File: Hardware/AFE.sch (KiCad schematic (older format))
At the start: 46 parts, among them U801 4069.HEF4069UBTT,118, U802 MCP47CXBX2

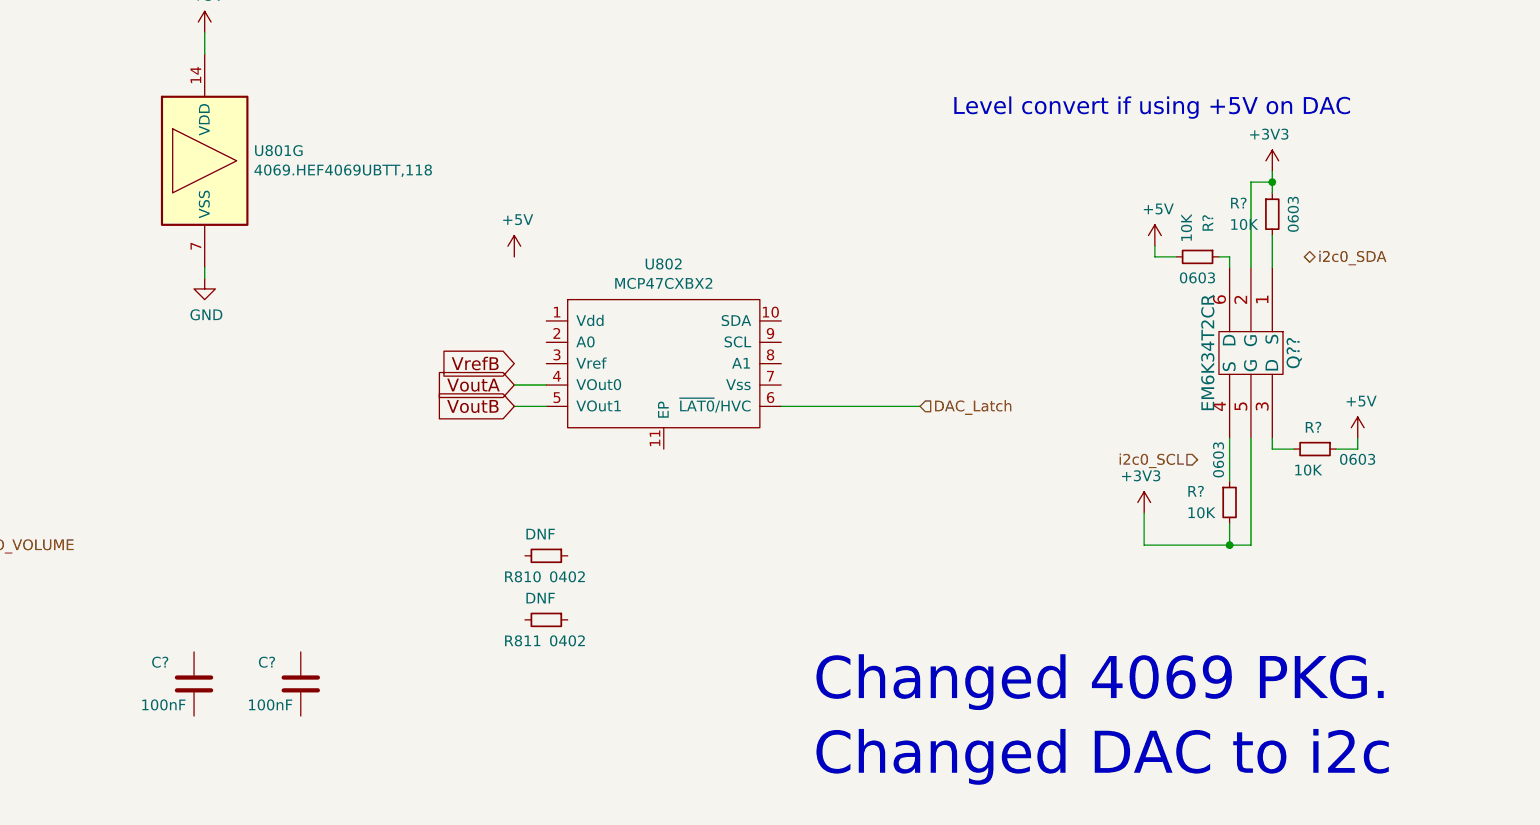
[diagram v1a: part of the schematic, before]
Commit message: Hooking up switches, some more connectivity.
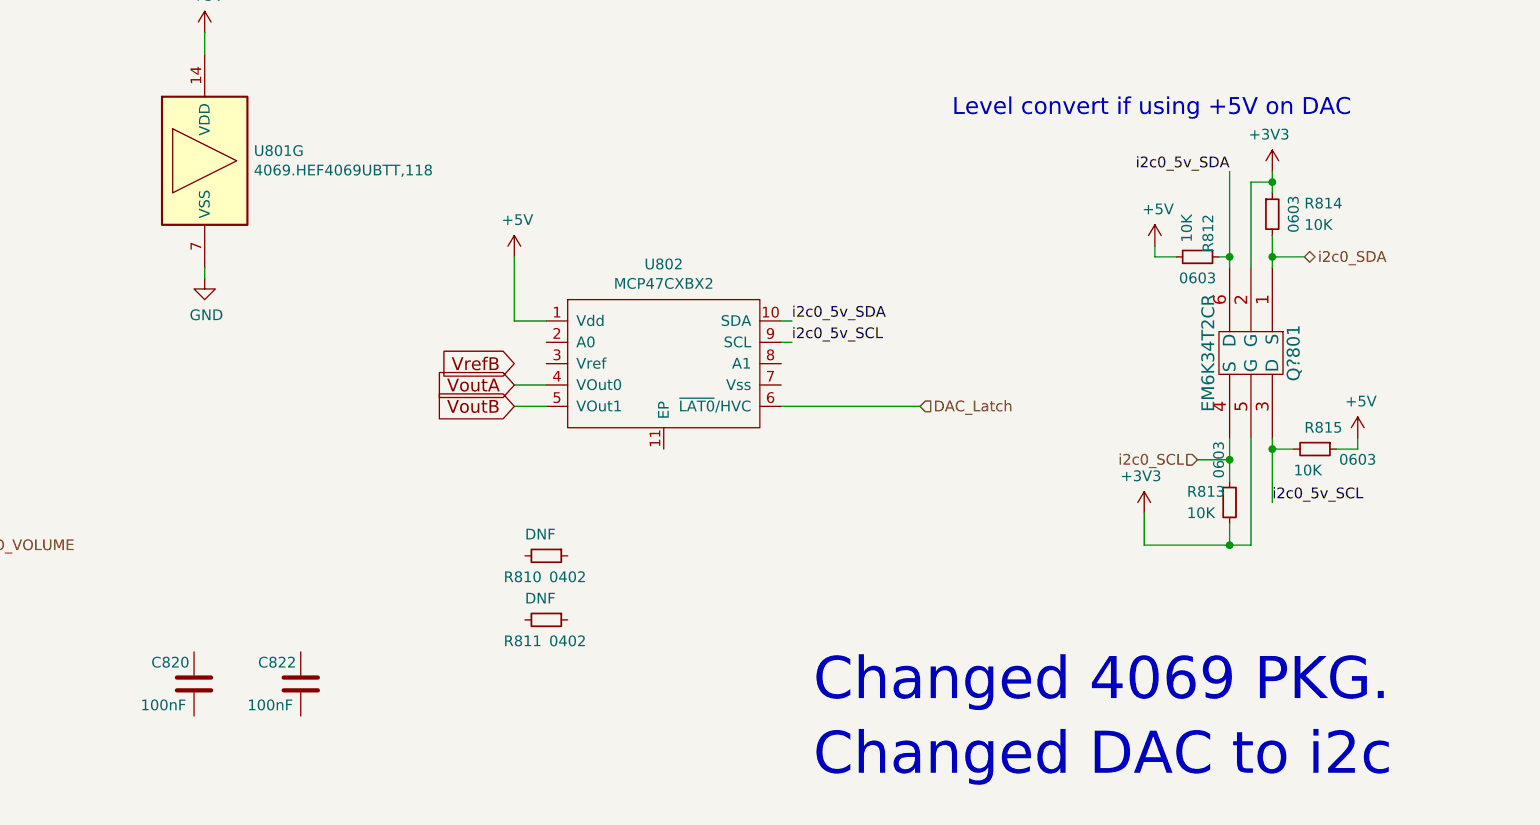
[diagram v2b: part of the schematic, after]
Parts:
- gave numbers to parts that had none: 7
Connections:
- net +5V: now also U802.1 (Vdd)
- net i2c0_SCL: now also Q?801.4 (S), R813.1
- net i2c0_SDA: now also Q?801.1 (S), R814.2
- net i2c0_5v_SDA: now reaches U802.10 (SDA)
- net i2c0_5v_SDA: now also Q?801.6 (D), R812.1
- net i2c0_5v_SCL: now reaches U802.9 (SCL)
- net i2c0_5v_SCL: now also Q?801.3 (D), R815.2
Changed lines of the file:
@@
 	1050 6900 1050 7000
 $Comp
-L OHMC2022:EM6K34T2CR Q??
+L OHMC2022:EM6K34T2CR Q?801
 U 1 1 613FBC97
 P 10200 4350
-F 0 "Q??" H 10200 4550 60  0000 C CNN
+F 0 "Q?801" H 10200 4550 60  0000 C CNN
 F 1 "EM6K34T2CR" H 10200 4150 60  0000 C CNN
 F 2 "OHMC2022:DualNFet.SOT563.EM6K34T2CR" H 11200 4590 60  0001 C CNN
@@
 $EndComp
 $Comp
-L Device:C C?
+L Device:C C822
 U 1 1 6140B8D2
 P 5750 5900
-F 0 "C?" H 5550 6000 50  0000 L CNN
+F 0 "C822" H 5550 6000 50  0000 L CNN
 F 1 "100nF" H 5500 5800 50  0000 L CNN
 F 2 "Capacitor_SMD:C_0603_1608Metric_Pad1.08x0.95mm_HandSolder" H 5788 5750 50  0001 C CNN
@@
 $EndComp
 $Comp
-L Device:C C?
+L Device:C C820
 U 1 1 6140CB4F
 P 5250 5900
-F 0 "C?" H 5050 6000 50  0000 L CNN
+F 0 "C820" H 5050 6000 50  0000 L CNN
 F 1 "100nF" H 5000 5800 50  0000 L CNN
 F 2 "Capacitor_SMD:C_0603_1608Metric_Pad1.08x0.95mm_HandSolder" H 5288 5750 50  0001 C CNN
@@
 AR Path="/611E335F/614210B0" Ref="R?"  Part="1"
 AR Path="/614210B0" Ref="R?"  Part="1"
-AR Path="/612429E8/614210B0" Ref="R?"  Part="1"
-F 0 "R?" H 10100 3750 50  0000 L CNN
-F 1 "10K" H 10100 3650 50  0000 L CNN
+AR Path="/612429E8/614210B0" Ref="R814"  Part="1"
+F 0 "R814" H 10450 3750 50  0000 L CNN
+F 1 "10K" H 10450 3650 50  0000 L CNN
 F 2 "Resistor_SMD:R_0603_1608Metric" V 10230 3700 50  0001 C CNN
 F 3 "~" H 10300 3700 50  0001 C CNN
@@
 AR Path="/611E335F/614261D7" Ref="R?"  Part="1"
 AR Path="/614261D7" Ref="R?"  Part="1"
-AR Path="/612429E8/614261D7" Ref="R?"  Part="1"
-F 0 "R?" H 9750 3950 50  0000 L CNN
+AR Path="/612429E8/614261D7" Ref="R812"  Part="1"
+F 0 "R812" H 9750 3950 50  0000 L CNN
 F 1 "10K" H 9750 3850 50  0000 L CNN
 F 2 "Resistor_SMD:R_0603_1608Metric" V 9880 3900 50  0001 C CNN
@@
 AR Path="/611E335F/61426AF8" Ref="R?"  Part="1"
 AR Path="/61426AF8" Ref="R?"  Part="1"
-AR Path="/612429E8/61426AF8" Ref="R?"  Part="1"
-F 0 "R?" V 10400 4750 50  0000 L CNN
+AR Path="/612429E8/61426AF8" Ref="R815"  Part="1"
+F 0 "R815" V 10400 4750 50  0000 L CNN
 F 1 "10K" V 10600 4700 50  0000 L CNN
 F 2 "Resistor_SMD:R_0603_1608Metric" V 10430 4800 50  0001 C CNN
@@
 AR Path="/611E335F/61427521" Ref="R?"  Part="1"
 AR Path="/61427521" Ref="R?"  Part="1"
-AR Path="/612429E8/61427521" Ref="R?"  Part="1"
-F 0 "R?" H 9900 5100 50  0000 L CNN
+AR Path="/612429E8/61427521" Ref="R813"  Part="1"
+F 0 "R813" H 9900 5100 50  0000 L CNN
 F 1 "10K" H 9900 5000 50  0000 L CNN
 F 2 "Resistor_SMD:R_0603_1608Metric" V 10030 5050 50  0001 C CNN
@@
 AR Path="/6123BB15/6142CCFA" Ref="#PWR?"  Part="1"
 AR Path="/611E335F/6142CCFA" Ref="#PWR?"  Part="1"
-AR Path="/612429E8/6142CCFA" Ref="#PWR?"  Part="1"
-F 0 "#PWR?" H 6750 3750 50  0001 C CNN
+AR Path="/612429E8/6142CCFA" Ref="#PWR0145"  Part="1"
+F 0 "#PWR0145" H 6750 3750 50  0001 C CNN
 F 1 "+5V" H 6765 4073 50  0000 C CNN
 F 2 "" H 6750 3900 50  0001 C CNN
@@
 AR Path="/6123BB15/6143609C" Ref="#PWR?"  Part="1"
 AR Path="/611E335F/6143609C" Ref="#PWR?"  Part="1"
-AR Path="/612429E8/6143609C" Ref="#PWR?"  Part="1"
-F 0 "#PWR?" H 10700 4600 50  0001 C CNN
+AR Path="/612429E8/6143609C" Ref="#PWR0146"  Part="1"
+F 0 "#PWR0146" H 10700 4600 50  0001 C CNN
 F 1 "+5V" H 10715 4923 50  0000 C CNN
 F 2 "" H 10700 4750 50  0001 C CNN
@@
 AR Path="/6123BB15/61436B56" Ref="#PWR?"  Part="1"
 AR Path="/611E335F/61436B56" Ref="#PWR?"  Part="1"
-AR Path="/612429E8/61436B56" Ref="#PWR?"  Part="1"
-F 0 "#PWR?" H 9750 3700 50  0001 C CNN
+AR Path="/612429E8/61436B56" Ref="#PWR0147"  Part="1"
+F 0 "#PWR0147" H 9750 3700 50  0001 C CNN
 F 1 "+5V" H 9765 4023 50  0000 C CNN
 F 2 "" H 9750 3850 50  0001 C CNN
@@
 AR Path="/611E3335/614785EE" Ref="#PWR?"  Part="1"
 AR Path="/614785EE" Ref="#PWR?"  Part="1"
-F 0 "#PWR?" H 9700 4950 50  0001 C CNN
+AR Path="/612429E8/614785EE" Ref="#PWR0148"  Part="1"
+F 0 "#PWR0148" H 9700 4950 50  0001 C CNN
 F 1 "+3V3" H 9715 5273 50  0000 C CNN
 F 2 "" H 9700 5100 50  0001 C CNN
@@
 AR Path="/611E3335/6147DD9F" Ref="#PWR?"  Part="1"
 AR Path="/6147DD9F" Ref="#PWR?"  Part="1"
-F 0 "#PWR?" H 10300 3350 50  0001 C CNN
+AR Path="/612429E8/6147DD9F" Ref="#PWR0149"  Part="1"
+F 0 "#PWR0149" H 10300 3350 50  0001 C CNN
 F 1 "+3V3" H 10315 3673 50  0000 C CNN
 F 2 "" H 10300 3500 50  0001 C CNN
@@
 	10100 5250 10100 5150
 Wire Wire Line
-	10100 4950 10100 4750
+	10100 4950 10100 4850
 Wire Wire Line
 	10200 4750 10200 5250
@@
 	10300 3550 10300 3600
 Wire Wire Line
-	10300 3800 10300 3950
+	10300 3800 10300 3900
+Wire Wire Line
+	6900 4200 6750 4200
+Wire Wire Line
+	6750 3900 6750 4200
+Wire Wire Line
+	9950 4850 10100 4850
+Connection ~ 10100 4850
+Wire Wire Line
+	10100 4850 10100 4750
+Wire Wire Line
+	10450 3900 10300 3900
+Connection ~ 10300 3900
+Wire Wire Line
+	10300 3900 10300 3950
+Text Label 8050 4300 0    50   ~ 0
+i2c0_5v_SCL
+Text Label 8050 4200 0    50   ~ 0
+i2c0_5v_SDA
+Wire Wire Line
+	8000 4300 8050 4300
+Wire Wire Line
+	8000 4200 8050 4200
+Text Label 10100 3500 2    50   ~ 0
+i2c0_5v_SDA
+Wire Wire Line
+	10100 3500 10100 3900
+Connection ~ 10100 3900
+Text Label 10300 5050 0    50   ~ 0
+i2c0_5v_SCL
+Wire Wire Line
+	10300 5050 10300 4800
+Connection ~ 10300 4800
 $EndSCHEMATC

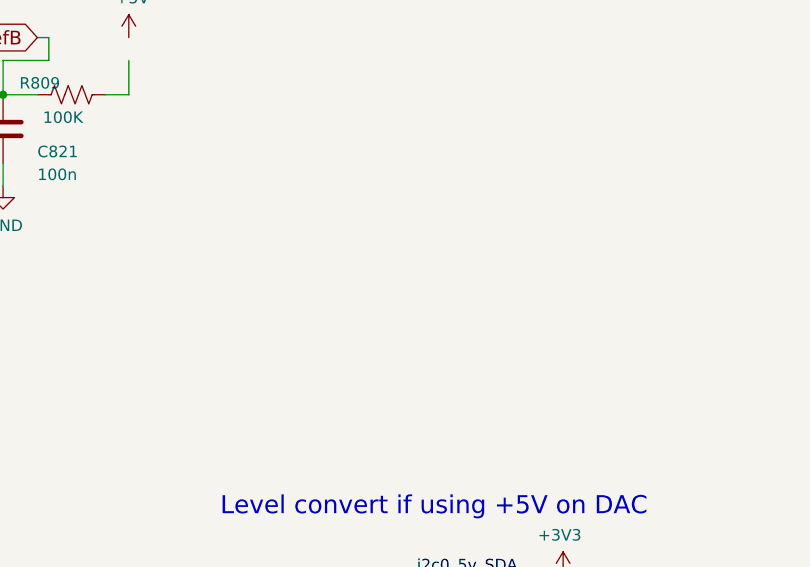
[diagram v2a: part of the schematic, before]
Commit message: Wiring up FPGA, picking pins.
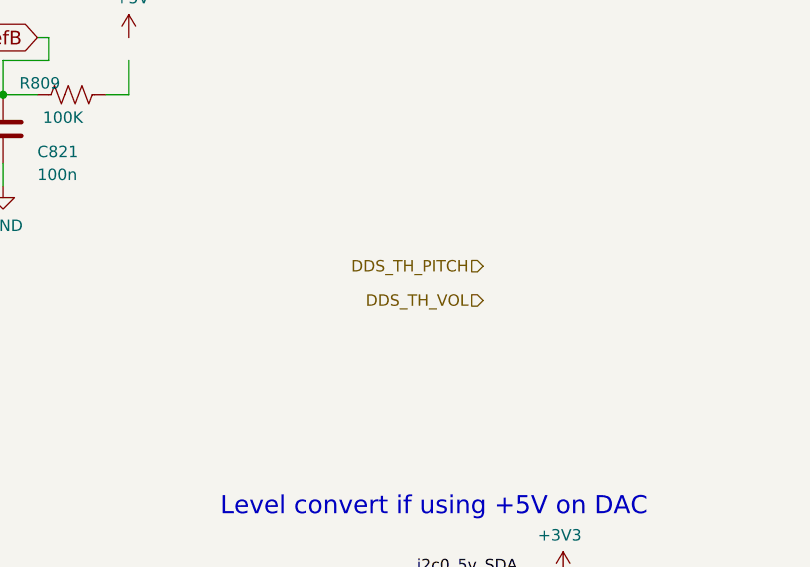
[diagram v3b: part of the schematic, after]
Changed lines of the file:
@@
 	10300 5050 10300 4800
 Connection ~ 10300 4800
+Text HLabel 9950 2150 0    50   Input ~ 0
+DDS_TH_PITCH
+Text HLabel 9950 2300 0    50   Input ~ 0
+DDS_TH_VOL
 $EndSCHEMATC

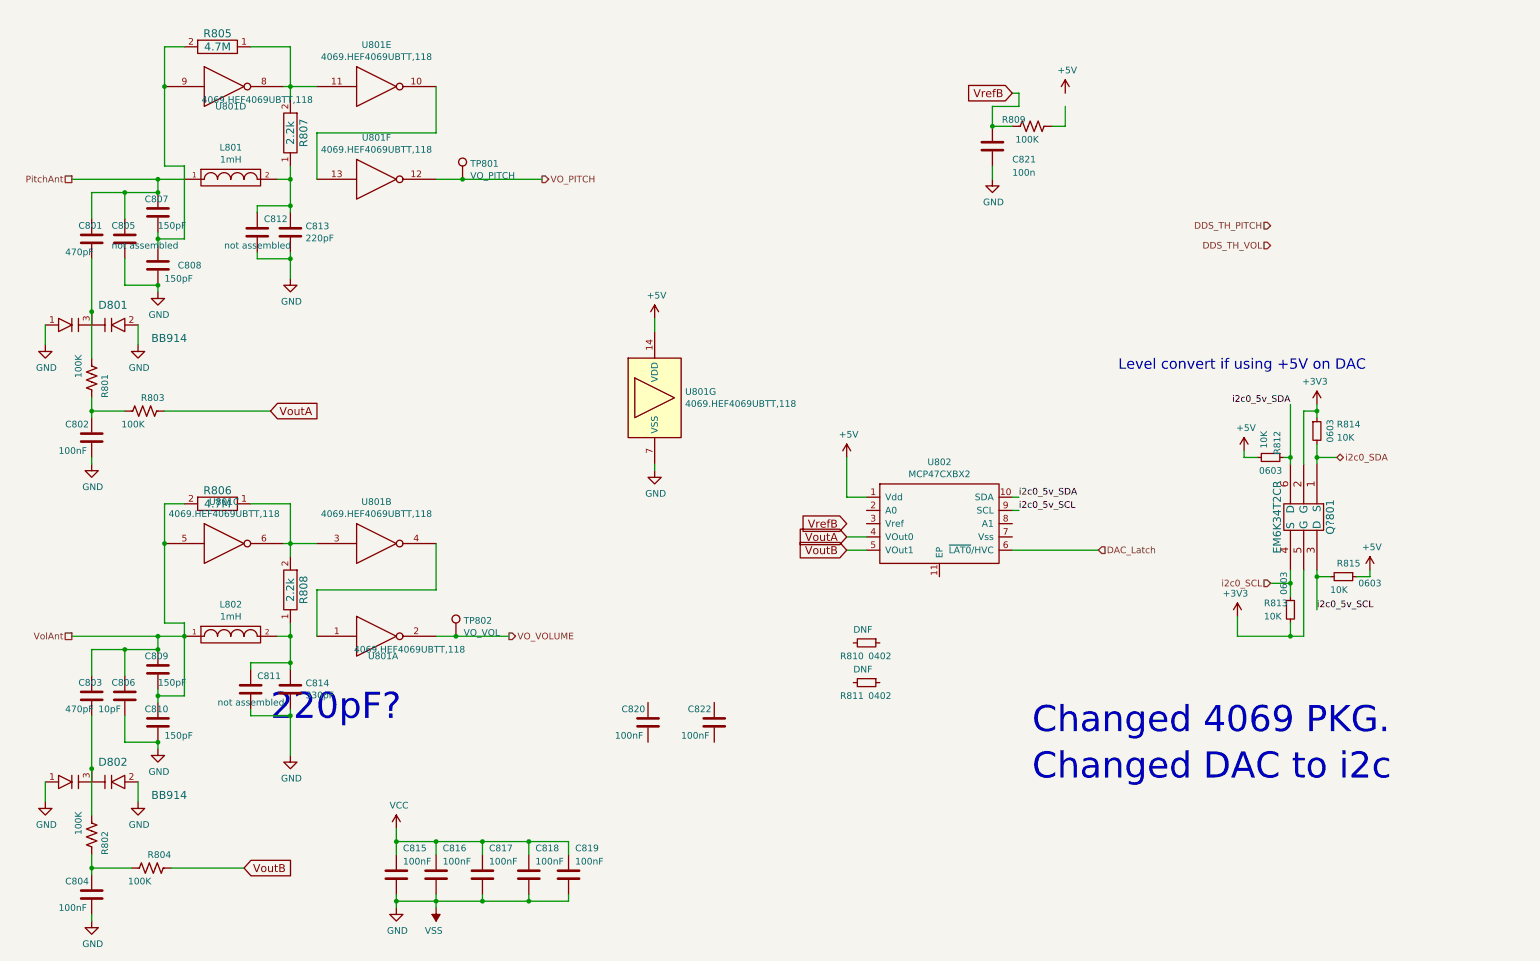
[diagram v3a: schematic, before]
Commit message: Schematic has proposed pin mapping on FPGA.
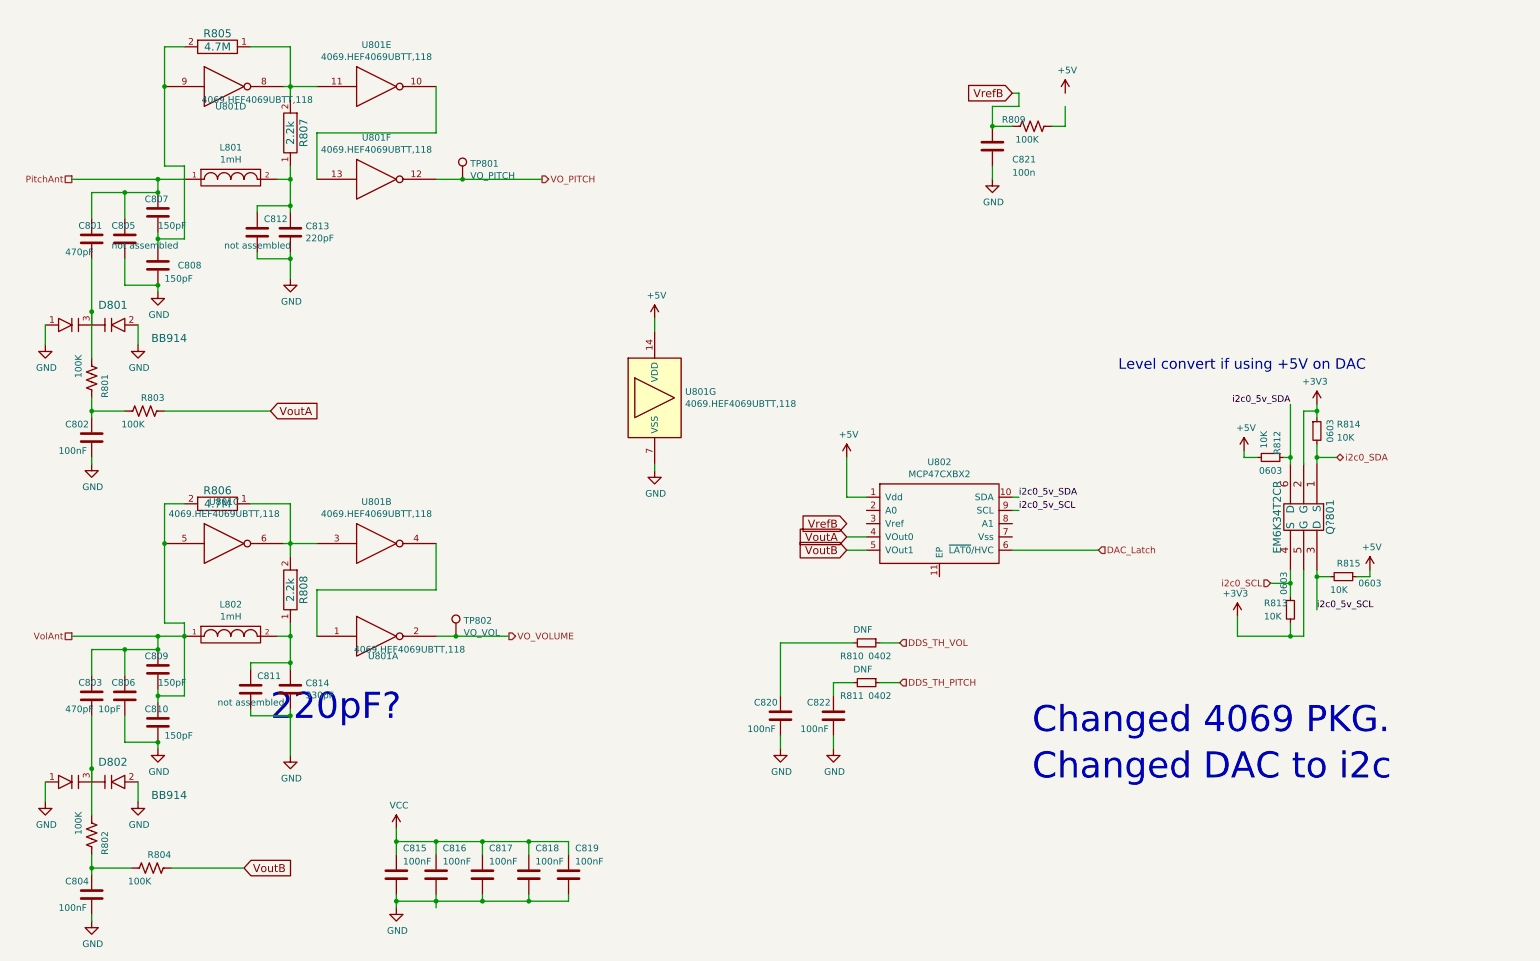
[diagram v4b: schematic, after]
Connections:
- net DDS_TH_PITCH: now also R811.1
- net DDS_TH_VOL: now also R810.1
- net GND: now also C820.2, C822.2; no longer U801.7 (VSS), U801.7 (VSS), U801.7 (VSS), U801.7 (VSS), U801.7 (VSS), U801.7 (VSS)
- net at C822.1: now also R811.2
- net at C820.1: now also R810.2
- new net VSS: U801.7 (VSS), U801.7 (VSS), U801.7 (VSS), U801.7 (VSS), U801.7 (VSS), U801.7 (VSS), U801.7 (VSS)
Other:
- moved on the sheet: C820, C822
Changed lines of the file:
@@
 	4650 6800 4650 6900
-$Comp
-L power:VSS #PWR0813
-U 1 1 5743F8AA
-P 3650 7300
-F 0 "#PWR0813" H 3650 7150 50  0001 C CNN
-F 1 "VSS" H 3668 7473 50  0000 C CNN
-F 2 "" H 3650 7300 50  0000 C CNN
-F 3 "" H 3650 7300 50  0000 C CNN
-	1    3650 7300
-	-1   0    0    1
-$EndComp
 $Comp
 L Device:C C811
@@
 L Device:C C822
 U 1 1 6140B8D2
-P 5750 5900
-F 0 "C822" H 5550 6000 50  0000 L CNN
-F 1 "100nF" H 5500 5800 50  0000 L CNN
-F 2 "Capacitor_SMD:C_0603_1608Metric_Pad1.08x0.95mm_HandSolder" H 5788 5750 50  0001 C CNN
-F 3 "" H 5750 5900 50  0000 C CNN
-	1    5750 5900
+P 6650 5850
+F 0 "C822" H 6450 5950 50  0000 L CNN
+F 1 "100nF" H 6400 5750 50  0000 L CNN
+F 2 "Capacitor_SMD:C_0603_1608Metric_Pad1.08x0.95mm_HandSolder" H 6688 5700 50  0001 C CNN
+F 3 "" H 6650 5850 50  0000 C CNN
+	1    6650 5850
 	1    0    0    -1
 $EndComp
@@
 L Device:C C820
 U 1 1 6140CB4F
-P 5250 5900
-F 0 "C820" H 5050 6000 50  0000 L CNN
-F 1 "100nF" H 5000 5800 50  0000 L CNN
-F 2 "Capacitor_SMD:C_0603_1608Metric_Pad1.08x0.95mm_HandSolder" H 5288 5750 50  0001 C CNN
-F 3 "" H 5250 5900 50  0000 C CNN
-	1    5250 5900
+P 6250 5850
+F 0 "C820" H 6050 5950 50  0000 L CNN
+F 1 "100nF" H 6000 5750 50  0000 L CNN
+F 2 "Capacitor_SMD:C_0603_1608Metric_Pad1.08x0.95mm_HandSolder" H 6288 5700 50  0001 C CNN
+F 3 "" H 6250 5850 50  0000 C CNN
+	1    6250 5850
 	1    0    0    -1
 $EndComp
@@
 	10300 5050 10300 4800
 Connection ~ 10300 4800
-Text HLabel 9950 2150 0    50   Input ~ 0
+Text HLabel 7150 5600 2    50   Input ~ 0
 DDS_TH_PITCH
-Text HLabel 9950 2300 0    50   Input ~ 0
+Text HLabel 7150 5300 2    50   Input ~ 0
 DDS_TH_VOL
+Wire Wire Line
+	7000 5600 7150 5600
+Wire Wire Line
+	7000 5300 7150 5300
+Wire Wire Line
+	6800 5600 6650 5600
+Wire Wire Line
+	6650 5600 6650 5700
+Wire Wire Line
+	6800 5300 6250 5300
+Wire Wire Line
+	6250 5300 6250 5700
+$Comp
+L power:GND #PWR0171
+U 1 1 6136E42E
+P 6650 6100
+F 0 "#PWR0171" H 6650 5850 50  0001 C CNN
+F 1 "GND" H 6658 5927 50  0000 C CNN
+F 2 "" H 6650 6100 50  0000 C CNN
+F 3 "" H 6650 6100 50  0000 C CNN
+	1    6650 6100
+	1    0    0    -1
+$EndComp
+$Comp
+L power:GND #PWR0172
+U 1 1 6136FBCA
+P 6250 6100
+F 0 "#PWR0172" H 6250 5850 50  0001 C CNN
+F 1 "GND" H 6258 5927 50  0000 C CNN
+F 2 "" H 6250 6100 50  0000 C CNN
+F 3 "" H 6250 6100 50  0000 C CNN
+	1    6250 6100
+	1    0    0    -1
+$EndComp
+Wire Wire Line
+	6250 6100 6250 6000
+Wire Wire Line
+	6650 6000 6650 6100
 $EndSCHEMATC
